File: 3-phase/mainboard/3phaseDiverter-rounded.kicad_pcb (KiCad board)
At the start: 2 copper layers, 144.8 x 120.6 mm, 107 parts, among them CN9 SMA, IC1 ATmega328-P, IC2 LM358, J0 FTDI, J1 RESET, J10 D10, J11 D11, J12 D12, J13 D13, J14 +5V, J15 +5V, J2 D2, J20 UnregDC, J3 D3, J30 regDC, J4 D4, J5 D5, J6 D6, J7 D7, J8 D8, J9 D9, X1 16MHz

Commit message: Some tuning
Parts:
- renumbered C9 to C10, C10 to C11, C11 to C20, C12 to C21, C8 to C6, C6 to C7, C7 to C8, C13 to C9, REF** to REF1, REF** to REF2, REF** to REF3, REF** to REF4

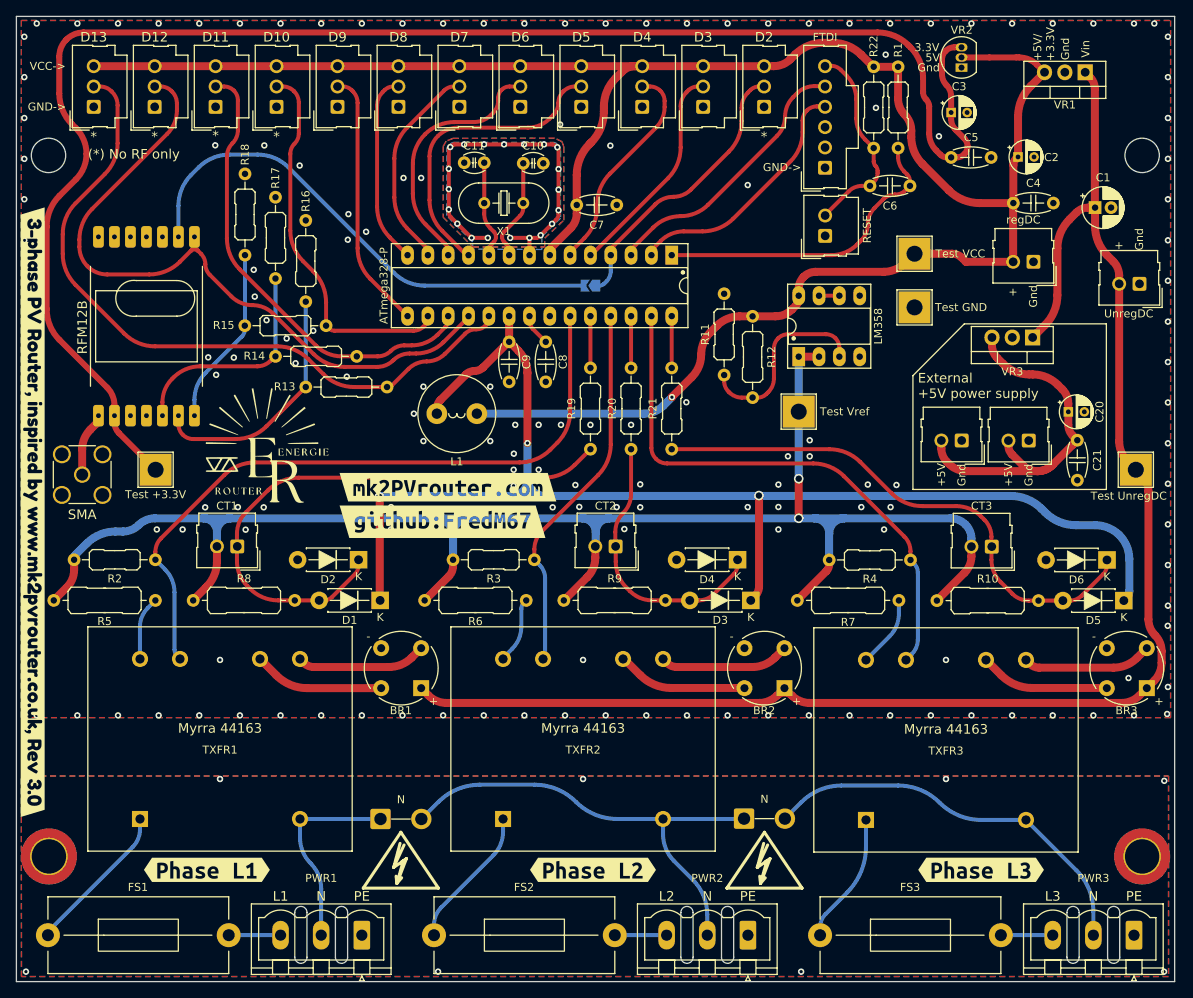
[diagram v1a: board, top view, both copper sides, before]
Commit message: Fix wrong pad & tuning
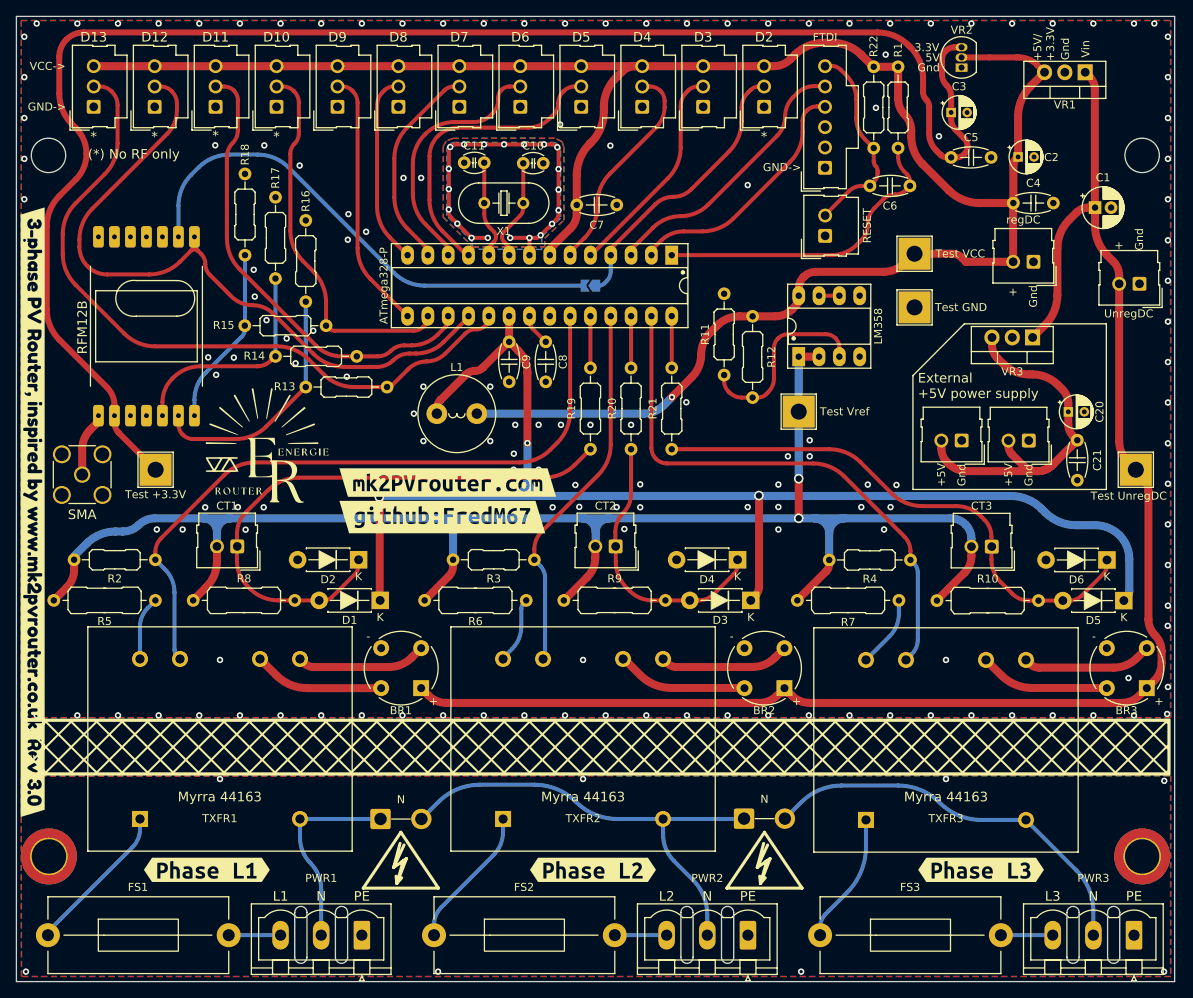
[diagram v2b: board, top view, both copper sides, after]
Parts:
- moved kibuzzard-6431D11C 0.58 mm to (69.2, 73.5)
- moved kibuzzard-64EB6544 0.58 mm to (68.5, 77.8)
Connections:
- REF2 pad 1: (no net) -> Earth

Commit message: Some tuning
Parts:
- removed kibuzzard-64C01F08: G***, kibuzzard-64C01F08
- added kibuzzard-65314627: G***, kibuzzard-65314627, F.Cu at (17.3, 77.2)
- moved C7 6.04 mm to (84.7, 36.5), turned to -90 degrees
- moved L1 2.88 mm to (73.4, 67.7), turned to 90 degrees
- moved C11 2.01 mm to (71.2, 35.5)
- moved C10 1.93 mm to (81.1, 35.5)
- moved C9 1.91 mm to (78.7, 55.9)
- moved X1 1.32 mm to (78.6, 39.9)
- moved TP3 1.27 mm to (127.5, 52.9)
- moved C8 0.64 mm to (82.0, 60.9)
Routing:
- net GND: track 46.2 -> 39.6 mm
- net AVCC: track 169.8 -> 174.9 mm, vias 3 -> 2
- net Net-(IC1-PB7/XTAL2/TOSC): track 12.3 -> 10.2 mm
- net Net-(IC1-PB6/XTAL1/TOSC1): track 12.7 -> 10.7 mm
- net /D5: track 37.9 -> 36.3 mm
- net VCC: track 270.4 -> 271.7 mm, vias 1 -> 0
- net Net-(IC1-AREF): track 3.99 -> 5.05 mm
- net /D6: track 31.8 -> 31.2 mm

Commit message: Tuning
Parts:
- added G***: LOGO, LOGO, B.Cu at (122.0, 73.6)
- added kibuzzard-6431D11C: G***, kibuzzard-6431D11C, B.Cu at (68.0, 73.4)
- added kibuzzard-64EB6544: G***, kibuzzard-64EB6544, B.Cu at (68.5, 78.0)
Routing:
- net Net-(IC2A-+): track 24.5 -> 18.9 mm
- net UnregDC+: track 192.9 -> 193.5 mm
